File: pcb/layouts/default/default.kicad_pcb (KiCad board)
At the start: 4 copper layers, 66.6 x 122.2 mm, 32 parts, among them U1 main.ato:Header1x22, U10 main.ato:Optocoupler, U11 main.ato:Optocoupler, U12 main.ato:Optocoupler, U13 main.ato:Optocoupler, U14 main.ato:Optocoupler, U15 270R, U16 270R, U17 270R, U18 270R, U19 270R, U2 main.ato:Header1x22, U20 270R, U21 10k, U22 33R, U23 33R, U24 10k, U25 10k, U26 10k, U27 10k, U28 main.ato:StatusLED, U3 main.ato:BoostModuleBS01, U4 main.ato:DisplaySocket, U5 main.ato:DisplaySocket, U6 main.ato:DisplaySocket, U7 main.ato:IsolatedPair, U8 main.ato:KeyfobSocket, U9 main.ato:SpareHeader

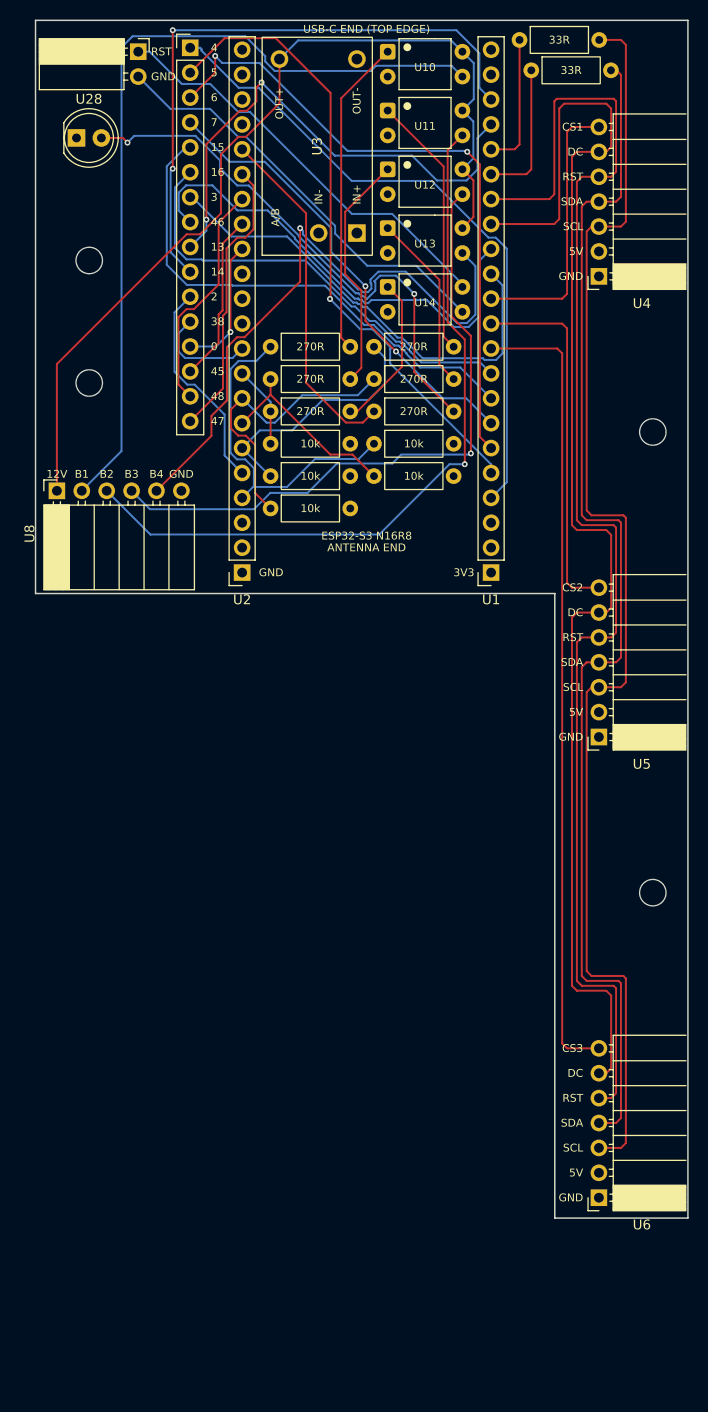
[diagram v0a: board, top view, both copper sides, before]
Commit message: feat(pcb): rev 2.3 - shrink board to 56.2x114.2mm, per-display RST
- Drop the 1x16 spare-GPIO header; move the keyfob socket to the west
  edge under the RST pair so the west strip is one RA socket deep.
- Pull the display column in from XR+11 to XR+6.25 (8 bus lanes at
  0.5mm). Both 33R stay flat: MOSI's on the top row, bus pads east of
  the right lanes.
- Display pitch 47 -> 43mm (37mm panel confirmed, 6mm gap).
- Per-display RST: RST1=GPIO10, RST2=GPIO16, RST3=GPIO15 (was shared
  GPIO10). RST1 hand-routed, RST2/3 Freerouted.
- Board refs derived from atopile instance names (J1-J7, PS1, U1-U5,
  R1-R13, D1) so removing a part no longer renumbers the rest.
- Scripts resolve paths from their own location (worktree-safe).
- Title block rev 2.3; docs updated, stale rev-3 notes fixed.

Was 66.6x122.2mm (-17% area). DRC 0/0, SPI topology check passes,
no 90-degree corners.

Co-Authored-By: Claude Opus 5.5 <noreply@anthropic.com>
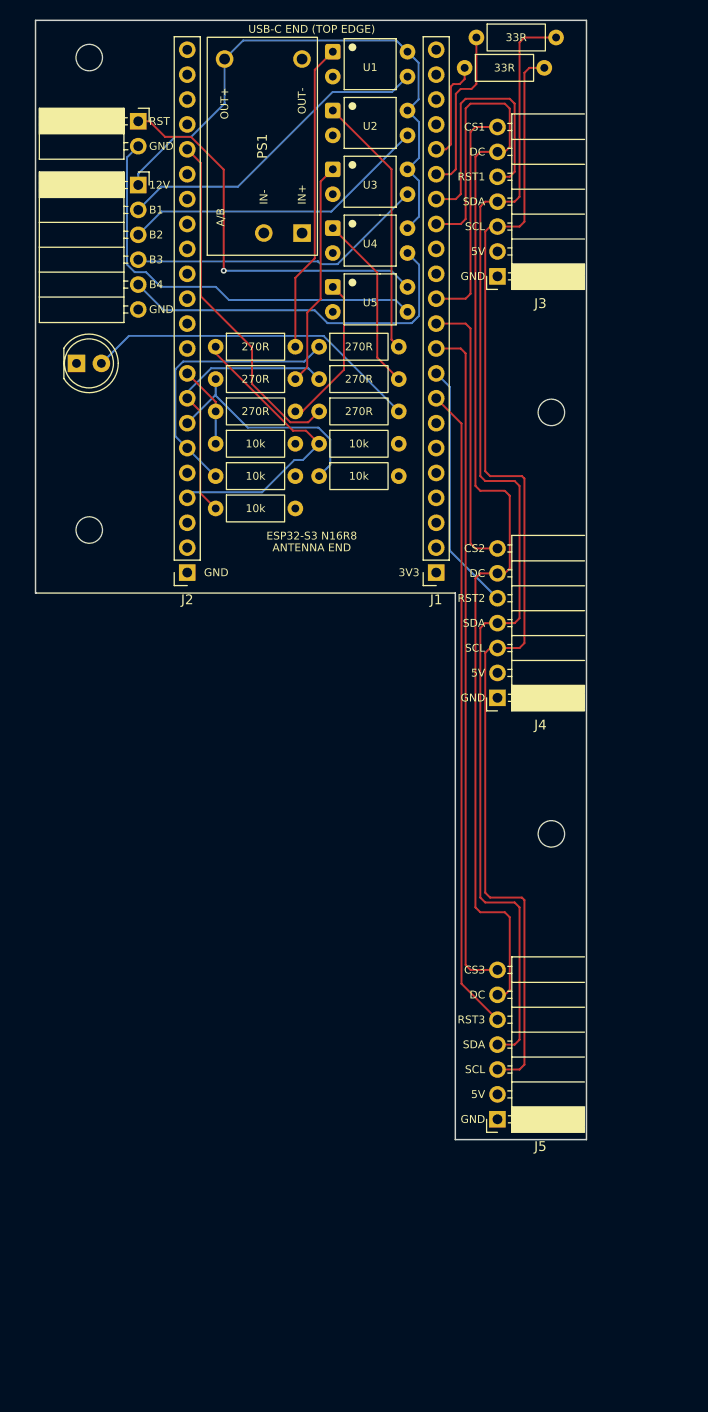
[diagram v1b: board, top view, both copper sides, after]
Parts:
- removed U10, U11, U12, U13, U14: main.ato:Optocoupler, DIP-4_W7.62mm
- removed U15, U16, U17, U18, U19, U20: 270R, R_Axial_DIN0207_L6.3mm_D2.5mm_P10.16mm_Horizontal
- removed U21, U24, U25, U26, U27: 10k, R_Axial_DIN0207_L6.3mm_D2.5mm_P10.16mm_Horizontal
- removed U22, U23: 33R, R_Axial_DIN0207_L6.3mm_D2.5mm_P10.16mm_Horizontal
- removed U28: main.ato:StatusLED, LED_D5.0mm
- removed U6: main.ato:DisplaySocket, PinSocket_1x07_P2.54mm_Horizontal
- removed U7: main.ato:IsolatedPair, PinSocket_1x02_P2.54mm_Horizontal
- removed U8: main.ato:KeyfobSocket, PinSocket_1x06_P2.54mm_Horizontal
- removed U9: main.ato:SpareHeader, PinHeader_1x16_P2.54mm_Vertical
- added D1: main.ato:StatusLED, LED_D5.0mm, F.Cu at (4.20, 35.0)
- added J1: main.ato:Header1x22, PinSocket_1x22_P2.54mm_Vertical, F.Cu at (40.9, 56.3)
- added J2: main.ato:Header1x22, PinSocket_1x22_P2.54mm_Vertical, F.Cu at (15.5, 56.3)
- added J3: main.ato:DisplaySocket, PinSocket_1x07_P2.54mm_Horizontal, F.Cu at (47.1, 26.1)
- added J4: main.ato:DisplaySocket, PinSocket_1x07_P2.54mm_Horizontal, F.Cu at (47.1, 69.1)
- added J5: main.ato:DisplaySocket, PinSocket_1x07_P2.54mm_Horizontal, F.Cu at (47.1, 112.1)
- added J6: main.ato:IsolatedPair, PinSocket_1x02_P2.54mm_Horizontal, F.Cu at (10.5, 10.3)
- added J7: main.ato:KeyfobSocket, PinSocket_1x06_P2.54mm_Horizontal, F.Cu at (10.5, 16.8)
- added PS1: main.ato:BoostModuleBS01, Boost_CKCS_BS01, F.Cu at (27.2, 21.7)
- added R1: 270R, R_Axial_DIN0207_L6.3mm_D2.5mm_P10.16mm_Horizontal, F.Cu at (18.4, 33.3)
- added R10: 10k, R_Axial_DIN0207_L6.3mm_D2.5mm_P10.16mm_Horizontal, F.Cu at (28.9, 43.2)
- added R11: 10k, R_Axial_DIN0207_L6.3mm_D2.5mm_P10.16mm_Horizontal, F.Cu at (18.4, 46.5)
- added R12: 10k, R_Axial_DIN0207_L6.3mm_D2.5mm_P10.16mm_Horizontal, F.Cu at (28.9, 46.5)
- added R13: 10k, R_Axial_DIN0207_L6.3mm_D2.5mm_P10.16mm_Horizontal, F.Cu at (18.4, 49.8)
- added R2: 270R, R_Axial_DIN0207_L6.3mm_D2.5mm_P10.16mm_Horizontal, F.Cu at (28.9, 33.3)
- added R3: 270R, R_Axial_DIN0207_L6.3mm_D2.5mm_P10.16mm_Horizontal, F.Cu at (18.4, 36.6)
- added R4: 270R, R_Axial_DIN0207_L6.3mm_D2.5mm_P10.16mm_Horizontal, F.Cu at (28.9, 36.6)
- added R5: 270R, R_Axial_DIN0207_L6.3mm_D2.5mm_P10.16mm_Horizontal, F.Cu at (18.4, 39.9)
- added R6: 270R, R_Axial_DIN0207_L6.3mm_D2.5mm_P10.16mm_Horizontal, F.Cu at (28.9, 39.9)
- added R7: 10k, R_Axial_DIN0207_L6.3mm_D2.5mm_P10.16mm_Horizontal, F.Cu at (18.4, 43.2)
- added R8: 33R, R_Axial_DIN0207_L6.3mm_D2.5mm_P10.16mm_Horizontal, F.Cu at (43.8, 4.85)
- added R9: 33R, R_Axial_DIN0207_L6.3mm_D2.5mm_P10.16mm_Horizontal, F.Cu at (45.0, 1.75)
- U1, U2: value main.ato:Header1x22 -> main.ato:Optocoupler; footprint PinSocket_1x22_P2.54mm_Vertical -> DIP-4_W7.62mm
- U3: value main.ato:BoostModuleBS01 -> main.ato:Optocoupler; footprint Boost_CKCS_BS01 -> DIP-4_W7.62mm
- U4, U5: value main.ato:DisplaySocket -> main.ato:Optocoupler; footprint PinSocket_1x07_P2.54mm_Horizontal -> DIP-4_W7.62mm
- moved U1 55.5 mm to (30.4, 3.20), turned to 0 degrees
- moved U5 53.3 mm to (30.4, 27.2), turned to 0 degrees
- moved U2 48.0 mm to (30.4, 9.20), turned to 0 degrees
- moved U4 27.6 mm to (30.4, 21.2), turned to 0 degrees
- moved MH1 20.7 mm to (5.50, 3.80)
- moved MH2 15.0 mm to (5.50, 52.0)
- moved MH4 12.0 mm to (52.6, 83.0)
- moved MH3 10.5 mm to (52.6, 40.0)
- moved U3 6.95 mm to (30.4, 15.2), turned to 0 degrees
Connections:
- U1 pad 1: vcc_3v3_1 -> opto1-anode
- U1 pad 2: vcc_3v3_2 -> gnd
- U1 pad 3: rst -> btn1
- U1 pad 4: gpio4 -> v12
- U2 pad 1: gnd -> opto2-anode
- U2 pad 2: txd0 -> gnd
- U2 pad 3: rxd0 -> btn2
- U2 pad 4: gpio1 -> v12
- U3 pad 1: v5 -> opto3-anode
- U3 pad 3: v12 -> btn3
- U3 pad 4: gnd -> v12
- U4 pad 1: gnd -> opto4-anode
- U4 pad 2: v5 -> gnd
- U4 pad 3: disp_sck -> btn4
- U4 pad 4: disp_mosi -> v12
- U5 pad 1: gnd -> opto5-anode
- U5 pad 2: v5 -> gnd
- U5 pad 3: disp_sck -> mb_rst_gnd
- U5 pad 4: disp_mosi -> mb_rst
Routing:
- net disp_rst: track 139.8 -> 0.00 mm
- net gpio4: track 67.0 -> 0.00 mm
- net gpio6: track 66.3 -> 0.00 mm, vias 2 -> 0
- net disp_rst3: track 0.00 -> 66.0 mm
- net gpio5: track 64.5 -> 0.00 mm, vias 1 -> 0
- net gpio14: track 63.0 -> 0.00 mm, vias 2 -> 0
- net gpio13: track 52.0 -> 0.00 mm, vias 2 -> 0
- net gpio15: track 52.0 -> 0.00 mm
- net btn1: track 84.6 -> 33.1 mm
- net gpio46: track 48.6 -> 0.00 mm
- net gpio3: track 47.6 -> 0.00 mm
- net gpio7: track 46.9 -> 0.00 mm, vias 2 -> 0
- net gpio16: track 45.9 -> 0.00 mm
- net btn2: track 76.2 -> 31.7 mm, vias 1 -> 0
- net v12: track 95.5 -> 58.3 mm
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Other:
- board size 66.6 x 122.2 mm -> 56.2 x 114.2 mm
- board text added: "RST1"
- board text added: "RST2"
- board text added: "RST3"
- board text removed: "0"
- board text removed: "13"
- board text removed: "14"
- board text removed: "15"
- board text removed: "16"
- board text removed: "2"
- board text removed: "3"
- board text removed: "38"
- board text removed: "4"
- board text removed: "45"
- board text removed: "46"
- board text removed: "47"
- board text removed: "48"
- board text removed: "5"
- board text removed: "6"
- board text removed: "7"

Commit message: feat(pcb): rev 2.4 - GMT024 2.4" panels, per-display backlight
- Display sockets 1x7 -> 1x8 for the GMT024-08-SPI8P (pad 1..8 = GND
  VCC SCL SDA RST DC CS BL); silkscreen adds BLn labels.
- Per-display backlight: BL1=GPIO7, BL2=GPIO6, BL3=GPIO5 -> pad 8,
  Freerouted on B.Cu (on/off or LEDC PWM per panel).
- Display pitch 43 -> 51.9mm (46.9mm panel + 5mm gap); board grows
  to 56.2 x 138.2mm. Display 1 centre moves to Y=23.45.
- Title block rev 2.4; README/Scripts.md updated.

DRC 0/0, SPI topology check passes, no 90-degree corners.

Co-Authored-By: Claude Opus 5.5 <noreply@anthropic.com>
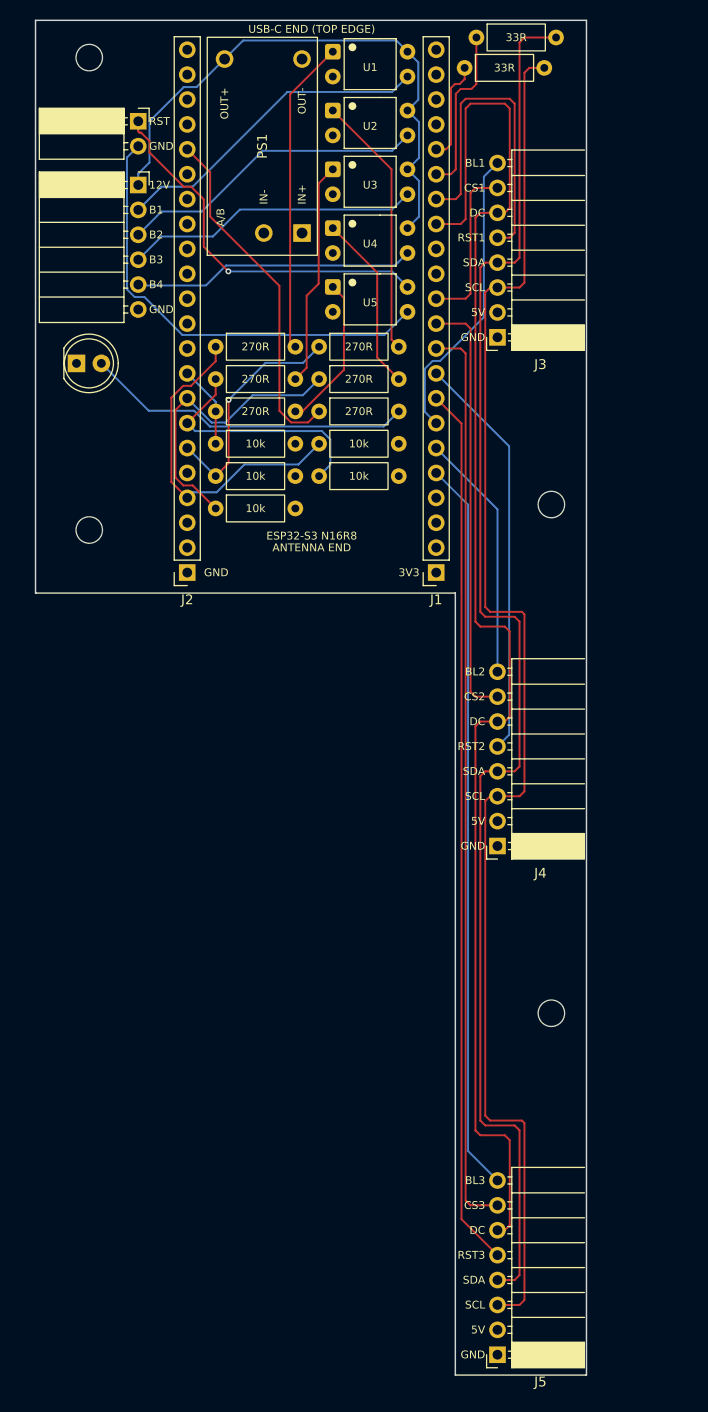
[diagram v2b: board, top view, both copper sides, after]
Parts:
- J3, J4, J5: footprint PinSocket_1x07_P2.54mm_Horizontal -> PinSocket_1x08_P2.54mm_Horizontal
- moved J5 24.0 mm to (47.1, 136.1)
- moved MH4 18.3 mm to (52.6, 101.3)
- moved J4 15.1 mm to (47.1, 84.2)
- moved MH3 9.40 mm to (52.6, 49.4)
- moved J3 6.22 mm to (47.1, 32.3)
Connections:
- J1 pad 5: gpio5 -> disp_bl3
- J1 pad 6: gpio6 -> disp_bl2
- J1 pad 7: gpio7 -> disp_bl1
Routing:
- net disp_bl3: track 0.00 -> 74.8 mm
- net disp_bl1: track 0.00 -> 30.5 mm
- net disp_bl2: track 0.00 -> 25.4 mm
- net disp_rst3: track 66.0 -> 90.0 mm
- net disp_mosi: track 121.8 -> 145.8 mm
- net gpio17: track 69.1 -> 93.1 mm
- net disp_dc: track 122.4 -> 146.5 mm
- net disp_sck: track 120.3 -> 144.4 mm
- net disp_rst2: track 25.5 -> 41.6 mm
- net gpio18: track 28.6 -> 43.7 mm
- net btn4: track 37.5 -> 28.9 mm
- net gpio8: track 23.2 -> 17.0 mm
- net disp_rst1: track 26.8 -> 33.0 mm
- net gpio42: track 28.2 -> 23.9 mm, vias 0 -> 1
- net mb_rst_gnd: track 43.2 -> 46.6 mm
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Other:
- board size 56.2 x 114.2 mm -> 56.2 x 138.2 mm
- board text added: "BL1"
- board text added: "BL2"
- board text added: "BL3"

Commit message: feat(pcb): rev 2.4b - 2-layer cost-down, F.Cu routing over B.Cu GND pour
- Scripts/board_config.py: COPPER_LAYERS (2 = rev 2.4b, 4 = rev 2.4),
  revision/date/title and Power net class values shared by the chain
- all routing on F.Cu; B.Cu is one unbroken GND pour carrying only 5
  short jumpers (3.8-8.0 mm, 27 mm total, 6 vias); pour 81.3% of raw
  board area, 99.3% of the no-jumper ideal; display bus still F.Cu, 0 vias
- 5V routed as a Power-class track (J1 -> west of J1 -> trunk under the
  display sockets, boost tee + one jumper); Power class in .kicad_pro
- optos turned 180deg and reordered U5,U1-U4 so outputs face the
  keyfob/RST sockets; R2/R3 swapped for planar anode lanes
- status LED GPIO21 -> GPIO2, R6 vertical in the west strip;
  BL1 GPIO7 -> GPIO13
- route_spi hand-routes RST2/3, BL1-3 and 5V on 2 layers; route_board
  two-pass Freerouting (F.Cu only, lock, then F.Cu+B.Cu)
- layout_board: fix pad 2 of rotated axial resistors; strip widened
  3.3 mm on 2 layers; GND pour pad clearance 0.3 mm
- DRC 0/0, SPI topology check passes, no 90deg corners

Co-Authored-By: Claude Opus 5.5 <noreply@anthropic.com>
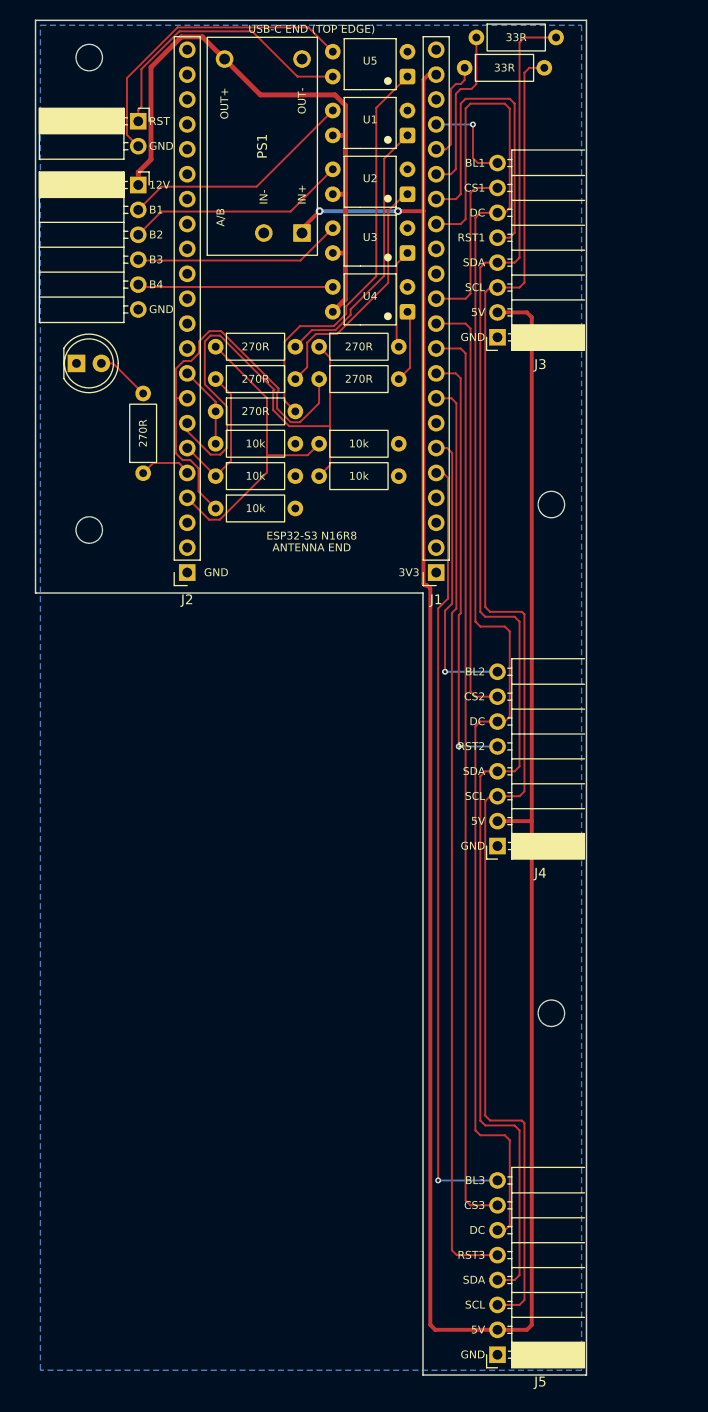
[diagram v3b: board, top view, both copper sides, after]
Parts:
- moved U5 22.8 mm to (38.0, 5.74), turned to 180 degrees
- moved R6 19.0 mm to (11.0, 46.2), turned to 90 degrees
- moved U1 11.4 mm to (38.0, 11.7), turned to 180 degrees
- moved U2 11.4 mm to (38.0, 17.7), turned to 180 degrees
- moved U3 11.4 mm to (38.0, 23.7), turned to 180 degrees
- moved U4 11.4 mm to (38.0, 29.7), turned to 180 degrees
- moved R2 11.1 mm to (18.4, 36.6)
- moved R3 11.1 mm to (28.9, 33.3)
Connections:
- J1 pad 19: gpio13 -> disp_bl1
- J1 pad 7: disp_bl1 -> gpio7
- R6 pad 1: gpio21 -> gpio2
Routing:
- net v5: track 0.00 -> 263.3 mm, vias 0 -> 2
- net gpio21: track 35.6 -> 0.00 mm
- net led_a: track 33.6 -> 5.53 mm
- net opto5-anode: track 15.6 -> 41.8 mm
- net gpio41: track 25.2 -> 50.3 mm
- net disp_bl1: track 30.5 -> 9.90 mm, vias 0 -> 1
- net mb_rst_gnd: track 46.6 -> 31.6 mm
- net opto3-anode: track 23.0 -> 10.1 mm
- net gpio40: track 30.3 -> 43.0 mm
- net opto4-anode: track 18.2 -> 7.44 mm
- net mb_rst: track 38.6 -> 28.5 mm, vias 1 -> 0
- net btn2: track 31.7 -> 22.6 mm
- net btn1: track 33.1 -> 24.1 mm
- net btn3: track 30.2 -> 21.3 mm
- net btn4: track 28.9 -> 19.9 mm
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- added copper zone on B.Cu, net gnd
- removed copper zone on In1.Cu, net gnd
- removed copper zone on In2.Cu, net v5
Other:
- outline, holes or cut-outs redrawn
- copper layers 4 -> 2

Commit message: feat(pcb): rev 3.0 - 45.7mm wide, RST/keyfob sockets below the module
- west strip removed: board 56.2 -> 45.7 x 138.2 mm; main body extends
  past the antenna end to Y=88 (inside the bounding box the strip
  already sets) holding J6 (RST pair, west edge), J7 (keyfob, turned
  90deg to face the bottom edge), D1 + R6 and a bottom-left hole;
  mounting holes now top-right, bottom-left + the two in the strip
- antenna keepout extended to Y=67.5 (DevKit ends at 66.3), all layers
- opto drive GPIOs remapped to J2's pin order: B1-B4 = GPIO39/40/41/42,
  motherboard RST = GPIO1 (was GPIO1/42/41/40 + GPIO39); opto slots back
  to U1-U5, resistor bank re-arranged for planar drive/pull-down/anode
- route_spi hand-routes every net (12V bus in the opto corridor, west
  channel to J6/J7/R6/D1, resistor bank); Freerouting is a safety net
- still 5 short B.Cu jumpers (27 mm), GND pour one piece, 99.4% of the
  no-jumper ideal; DRC 0/0, SPI topology OK, every corner 45deg

Co-Authored-By: Claude Opus 5.5 <noreply@anthropic.com>
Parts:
- moved J7 61.3 mm to (19.0, 77.5), turned to 90 degrees
- moved J6 60.4 mm to (21.0, 69.8)
- moved D1 50.0 mm to (38.9, 71.0), turned to 180 degrees
- moved MH1 46.9 mm to (52.0, 9.70)
- moved MH2 33.1 mm to (14.0, 84.0)
- moved R6 28.6 mm to (25.2, 71.0), turned to 0 degrees
- moved U5 24.0 mm to (38.0, 29.7)
- moved R11 13.2 mm to (29.8, 39.9)
- moved R5 13.2 mm to (29.8, 33.3)
- moved R3 12.4 mm to (18.4, 39.9)
- moved R12 11.1 mm to (18.4, 43.2)
- moved R7 6.60 mm to (18.4, 49.8)
- moved U1 6.00 mm to (38.0, 5.74)
- moved U3 6.00 mm to (38.0, 17.7)
- moved U4 6.00 mm to (38.0, 23.7)
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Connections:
- R1 pad 1: gpio1 -> gpio39
- R2 pad 1: gpio42 -> gpio40
- R4 pad 1: gpio40 -> gpio42
- R5 pad 1: gpio39 -> gpio1
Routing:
- net btn1: track 24.1 -> 99.7 mm
- net btn2: track 22.6 -> 97.4 mm
- net btn3: track 21.3 -> 94.2 mm
- net v12: track 62.0 -> 134.0 mm
- net btn4: track 19.9 -> 86.8 mm
- net gpio41: track 50.3 -> 6.44 mm
- net opto5-anode: track 41.8 -> 3.56 mm
- net mb_rst_gnd: track 31.6 -> 69.0 mm
- net mb_rst: track 28.5 -> 63.1 mm
- net gpio2: track 5.46 -> 36.0 mm
- net gpio40: track 43.0 -> 17.1 mm
- net gpio42: track 15.3 -> 39.4 mm
- net opto3-anode: track 10.1 -> 31.8 mm
- net gpio39: track 8.38 -> 25.1 mm
- net opto1-anode: track 27.7 -> 38.1 mm
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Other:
- board size 56.2 x 138.2 mm -> 45.7 x 138.2 mm

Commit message: feat(pcb): rev 3.1 - BL1 on GPIO3, no B.Cu jumper under SCK/MOSI
- BL1 moves from GPIO13 (J1 pin 19, inside the SCK/MOSI riser loop) to
  GPIO3 (pin 13, below the bus); its one B.Cu jumper now crosses only
  DC + CS1, so the GND pour under both fast lines is unbroken
- Firmware: TFT_BL = 3 in every sketch
- "USB-C END" marker moved off the 12V bus
- render_board.py draws silkscreen on top of copper, as fabbed
- DRC 0/0, netlist parity OK, bus still F.Cu-only daisy chain

Co-Authored-By: Claude Opus 5.5 <noreply@anthropic.com>
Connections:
- J1 pad 13: gpio3 -> disp_bl1
- J1 pad 19: disp_bl1 -> gpio13
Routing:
- net disp_bl1: track 9.90 -> 14.6 mm, vias 1 -> 2
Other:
- board text added: "USB-C END"
- board text removed: "USB-C END (TOP EDGE)"
